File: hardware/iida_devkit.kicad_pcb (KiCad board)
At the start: 4 copper layers, 0 parts

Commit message: HW: Fix 3D models for components
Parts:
- added AE1: U.FL-R-SMT-1(10), Connector_Coaxial:U.FL_Hirose_U.FL-R-SMT-1_Vertical, F.Cu at (176.2, 138.7)
- added AE2: PCB antenna, PCB_antenna:800MHz_antenna, F.Cu at (163.4, 134.9)
- added C1: 4700 pF, Capacitor_SMD:C_0603_1608Metric_Pad1.08x0.95mm_HandSolder, F.Cu at (130.6, 115.9)
- added C10: 4.7 µF, Capacitor_SMD:C_0603_1608Metric_Pad1.08x0.95mm_HandSolder, F.Cu at (135.3, 61.2)
- added C11: 8 pF, Capacitor_SMD:C_0603_1608Metric_Pad1.08x0.95mm_HandSolder, F.Cu at (135.3, 63.7)
- added C12: 8 pF, Capacitor_SMD:C_0603_1608Metric_Pad1.08x0.95mm_HandSolder, F.Cu at (135.3, 66.2)
- added C13: 8 pF, Capacitor_SMD:C_0603_1608Metric_Pad1.08x0.95mm_HandSolder, F.Cu at (135.3, 68.8)
- added C14: 8 pF, Capacitor_SMD:C_0603_1608Metric_Pad1.08x0.95mm_HandSolder, F.Cu at (135.3, 71.3)
- added C15: 4.7 µF, Capacitor_SMD:C_0603_1608Metric_Pad1.08x0.95mm_HandSolder, F.Cu at (135.3, 73.8)
- added C16: 0.1 µF, Capacitor_SMD:C_0603_1608Metric_Pad1.08x0.95mm_HandSolder, F.Cu at (135.3, 76.3)
- added C17: 4.7 µF, Capacitor_SMD:C_0603_1608Metric_Pad1.08x0.95mm_HandSolder, F.Cu at (139.7, 61.2)
- added C18: 0.1 µF, Capacitor_SMD:C_0603_1608Metric_Pad1.08x0.95mm_HandSolder, F.Cu at (139.7, 63.7)
- added C19: 0.1 µF, Capacitor_SMD:C_0603_1608Metric_Pad1.08x0.95mm_HandSolder, F.Cu at (139.7, 66.2)
- added C2: 100 µF, Capacitor_SMD:CP_Elec_5x5.3, F.Cu at (139.5, 143.2)
- added C20: 4.7 µF, Capacitor_SMD:C_0603_1608Metric_Pad1.08x0.95mm_HandSolder, F.Cu at (139.7, 68.8)
- added C21: 0.1 µF, Capacitor_SMD:C_0603_1608Metric_Pad1.08x0.95mm_HandSolder, F.Cu at (139.7, 71.3)
- added C22: 0.1 µF, Capacitor_SMD:C_0603_1608Metric_Pad1.08x0.95mm_HandSolder, F.Cu at (139.7, 73.8)
- added C23: 0.1 µF, Capacitor_SMD:C_0603_1608Metric_Pad1.08x0.95mm_HandSolder, F.Cu at (139.7, 76.3)
- added C24: 0.1 µF, Capacitor_SMD:C_0603_1608Metric_Pad1.08x0.95mm_HandSolder, F.Cu at (181.7, 61.2)
- added C25: 68 pF, Capacitor_SMD:C_0603_1608Metric_Pad1.08x0.95mm_HandSolder, F.Cu at (181.7, 63.7)
- added C26: 15 pF, Capacitor_SMD:C_0603_1608Metric_Pad1.08x0.95mm_HandSolder, F.Cu at (181.7, 66.2)
- added C27: 0.1 µF, Capacitor_SMD:C_0603_1608Metric_Pad1.08x0.95mm_HandSolder, F.Cu at (181.7, 68.8)
- added C28: 0.01 µF, Capacitor_SMD:C_0603_1608Metric_Pad1.08x0.95mm_HandSolder, F.Cu at (181.7, 71.3)
- added C29: 0.1 µF, Capacitor_SMD:C_0603_1608Metric_Pad1.08x0.95mm_HandSolder, F.Cu at (181.7, 73.8)
- added C3: 0.1 µF, Capacitor_SMD:C_0603_1608Metric_Pad1.08x0.95mm_HandSolder, F.Cu at (130.6, 118.4)
- added C30: 0.1 µF, Capacitor_SMD:C_0603_1608Metric_Pad1.08x0.95mm_HandSolder, F.Cu at (186.1, 61.2)
- added C31: 10 µF, Capacitor_SMD:C_0603_1608Metric_Pad1.08x0.95mm_HandSolder, F.Cu at (186.1, 63.7)
- added C32: 0.1 µF, Capacitor_SMD:C_0603_1608Metric_Pad1.08x0.95mm_HandSolder, F.Cu at (186.1, 66.2)
- added C33: 33 pF, Capacitor_SMD:C_0603_1608Metric_Pad1.08x0.95mm_HandSolder, F.Cu at (183.2, 96.8)
- added C34: 33 pF, Capacitor_SMD:C_0603_1608Metric_Pad1.08x0.95mm_HandSolder, F.Cu at (183.2, 99.3)
- added C35: 33 pF, Capacitor_SMD:C_0603_1608Metric_Pad1.08x0.95mm_HandSolder, F.Cu at (183.2, 101.8)
- added C36: 33 pF, Capacitor_SMD:C_0603_1608Metric_Pad1.08x0.95mm_HandSolder, F.Cu at (183.2, 104.3)
- added C37: 0.1 µF, Capacitor_SMD:C_0603_1608Metric_Pad1.08x0.95mm_HandSolder, F.Cu at (183.2, 106.8)
- added C38: 33 pF, Capacitor_SMD:C_0603_1608Metric_Pad1.08x0.95mm_HandSolder, F.Cu at (181.2, 136.9)
- added C4: 0.1 µF, Capacitor_SMD:C_0603_1608Metric_Pad1.08x0.95mm_HandSolder, F.Cu at (130.6, 121.0)
- added C5: 0.1 µF, Capacitor_SMD:C_0603_1608Metric_Pad1.08x0.95mm_HandSolder, F.Cu at (130.6, 123.5)
- added C6: 4.7 µF, Capacitor_SMD:C_0603_1608Metric_Pad1.08x0.95mm_HandSolder, F.Cu at (130.6, 126.0)
- added C7: 4.7 µF, Capacitor_SMD:C_0603_1608Metric_Pad1.08x0.95mm_HandSolder, F.Cu at (130.6, 128.5)
- added C8: 4.7 µF, Capacitor_SMD:C_0603_1608Metric_Pad1.08x0.95mm_HandSolder, F.Cu at (134.9, 115.9)
- added C9: 4.7 µF, Capacitor_SMD:C_0603_1608Metric_Pad1.08x0.95mm_HandSolder, F.Cu at (134.9, 118.4)
- added D1: CDBA140LL-HF, Diode_SMD:D_SMA_Handsoldering, F.Cu at (123.4, 109.8)
- added D2: CDBA140LL-HF, Diode_SMD:D_SMA_Handsoldering, F.Cu at (123.4, 114.3)
- added D3: CDBA140LL-HF, Diode_SMD:D_SMA_Handsoldering, F.Cu at (123.4, 118.8)
- added D4: CDBA140LL-HF, Diode_SMD:D_SMA_Handsoldering, F.Cu at (123.4, 123.4)
- added D5: CDBA140LL-HF, Diode_SMD:D_SMA_Handsoldering, F.Cu at (123.4, 128.0)
- added F1: 3A, Fuse:Fuse_0805_2012Metric_Pad1.15x1.40mm_HandSolder, F.Cu at (120.7, 142.8)
- added F2: 3A, Fuse:Fuse_0805_2012Metric_Pad1.15x1.40mm_HandSolder, F.Cu at (120.7, 145.8)
- added FB1: 120 Ω @ 100 MHz, Resistor_SMD:R_0603_1608Metric_Pad0.98x0.95mm_HandSolder, F.Cu at (134.9, 121.0)
- added FB2: 120 Ω @ 100 MHz, Resistor_SMD:R_0603_1608Metric_Pad0.98x0.95mm_HandSolder, F.Cu at (144.0, 61.2)
- added FB3: 260 Ω @ 1 GHz, Resistor_SMD:R_0603_1608Metric_Pad0.98x0.95mm_HandSolder, F.Cu at (186.1, 68.8)
- added FID1: Fiducial, Fiducial:Fiducial_1mm_Mask2mm, F.Cu at (195.1, 97.3)
- added FID2: Fiducial, Fiducial:Fiducial_1mm_Mask2mm, F.Cu at (195.1, 100.9)
- added FID3: Fiducial, Fiducial:Fiducial_1mm_Mask2mm, F.Cu at (195.1, 104.4)
- added H1: MountingHole_Pad, MountingHole:MountingHole_2.2mm_M2_Pad_Via, F.Cu at (190.4, 98.5)
- added H2: MountingHole_Pad, MountingHole:MountingHole_2.2mm_M2_Pad_Via, F.Cu at (190.4, 104.5)
- added H3: MountingHole_Pad, MountingHole:MountingHole_2.2mm_M2_Pad_Via, F.Cu at (190.4, 110.4)
- added H4: MountingHole_Pad, MountingHole:MountingHole_2.2mm_M2_Pad_Via, F.Cu at (190.4, 116.4)
- added J1: B2B-PH-K-S, Connector_JST:JST_PH_B2B-PH-K_1x02_P2.00mm_Vertical, F.Cu at (147.0, 142.4)
- added J10: PRPC001DAAN-RC, Connector_PinHeader_2.54mm:PinHeader_1x02_P2.54mm_Vertical, F.Cu at (154.7, 91.3)
- added J11: PRPC006SAAN-RC, Connector_PinHeader_2.54mm:PinHeader_1x06_P2.54mm_Vertical, F.Cu at (157.5, 62.3)
- added J12: PRPC004SAAN-RC, Connector_PinHeader_2.54mm:PinHeader_1x04_P2.54mm_Vertical, F.Cu at (136.9, 94.8)
- added J13: PRPC001DAAN-RC, Connector_PinHeader_2.54mm:PinHeader_1x02_P2.54mm_Vertical, F.Cu at (194.9, 62.3)
- added J14: PRPC006SAAN-RC, Connector_PinHeader_2.54mm:PinHeader_1x06_P2.54mm_Vertical, F.Cu at (164.2, 97.9)
- added J15: G85D1160022HHR, G85D1160022HHR:AMPHENOL_G85D1160022HHR, F.Cu at (173.8, 104.2)
- added J2: USB4110-GF-A, Connector_USB:USB_C_Receptacle_GCT_USB4110, F.Cu at (142.3, 135.0)
- added J3: PRPC001DAAN-RC, Connector_PinHeader_2.54mm:PinHeader_1x02_P2.54mm_Vertical, F.Cu at (130.7, 109.8)
- added J4: PRPC001DAAN-RC, Connector_PinHeader_2.54mm:PinHeader_1x02_P2.54mm_Vertical, F.Cu at (135.4, 109.8)
- added J5: PRPC001DAAN-RC, Connector_PinHeader_2.54mm:PinHeader_1x02_P2.54mm_Vertical, F.Cu at (140.0, 109.8)
- added J6: PRPC001DAAN-RC, Connector_PinHeader_2.54mm:PinHeader_1x02_P2.54mm_Vertical, F.Cu at (144.7, 109.8)
- added J7: PRPC001DAAN-RC, Connector_PinHeader_2.54mm:PinHeader_1x02_P2.54mm_Vertical, F.Cu at (149.3, 109.8)
- added J8: SBH11-NBPC-D05-SM-BK, Connector_PinHeader_2.54mm:PinHeader_2x05_P2.54mm_Vertical_SMD, F.Cu at (134.8, 85.0)
- added J9: PRPC006SAAN-RC, Connector_PinHeader_2.54mm:PinHeader_1x06_P2.54mm_Vertical, F.Cu at (152.9, 62.3)
- added JP1: SolderJumper_3_Open, Jumper:SolderJumper-3_P2.0mm_Open_TrianglePad1.0x1.5mm, F.Cu at (170.1, 137.5)
- added L1: 2.7 µH, Inductor_SMD:L_Bourns-SRU8028_8.0x8.0mm, F.Cu at (147.1, 119.6)
- added L2: 39 nH, Inductor_SMD:L_0603_1608Metric_Pad1.05x0.95mm_HandSolder, F.Cu at (181.2, 139.4)
- added LED1: 150141YS73100, LED_SMD:LED_PLCC_2835_Handsoldering, F.Cu at (150.4, 126.7)
- added LED2: 150141YS73100, LED_SMD:LED_PLCC_2835_Handsoldering, F.Cu at (131.5, 94.6)
- added LED3: 150141YS73100, LED_SMD:LED_PLCC_2835_Handsoldering, F.Cu at (131.5, 99.0)
- added LED4: 150141YS73100, LED_SMD:LED_PLCC_2835_Handsoldering, F.Cu at (131.5, 103.3)
- added LED5: 150141YS73100, LED_SMD:LED_PLCC_2835_Handsoldering, F.Cu at (164.9, 89.7)
- added Q1: IRLML2246TRPBF, Package_TO_SOT_SMD:SC-59_Handsoldering, F.Cu at (131.7, 132.2)
- added Q2: DMN2046U-7, Package_TO_SOT_SMD:SC-59_Handsoldering, F.Cu at (131.7, 137.1)
- added Q3: DMN2046U-7, Package_TO_SOT_SMD:SC-59_Handsoldering, F.Cu at (131.7, 141.9)
- added Q4: IRLML2246TRPBF, Package_TO_SOT_SMD:SC-59_Handsoldering, F.Cu at (131.7, 146.7)
- added Q5: IRLML2246TRPBF, Package_TO_SOT_SMD:SC-59_Handsoldering, F.Cu at (190.0, 77.5)
- added Q6: MMBT3904, Package_TO_SOT_SMD:SC-59_Handsoldering, F.Cu at (190.0, 82.4)
- added R1: 1 MΩ, Resistor_SMD:R_1206_3216Metric_Pad1.30x1.75mm_HandSolder, F.Cu at (121.3, 136.4)
- added R10: 220 kΩ, Resistor_SMD:R_0603_1608Metric_Pad0.98x0.95mm_HandSolder, F.Cu at (139.3, 126.0)
- added R11: 20 Ω, Resistor_SMD:R_0603_1608Metric_Pad0.98x0.95mm_HandSolder, F.Cu at (144.0, 63.7)
- added R12: 20 Ω, Resistor_SMD:R_0603_1608Metric_Pad0.98x0.95mm_HandSolder, F.Cu at (144.0, 66.2)
- added R13: 0 Ω, Resistor_SMD:R_0805_2012Metric_Pad1.20x1.40mm_HandSolder, F.Cu at (130.8, 61.5)
- added R14: 0 Ω, Resistor_SMD:R_0805_2012Metric_Pad1.20x1.40mm_HandSolder, F.Cu at (130.8, 64.4)
- added R15: 2.2 kΩ, Resistor_SMD:R_0603_1608Metric_Pad0.98x0.95mm_HandSolder, F.Cu at (144.0, 68.8)
- added R16: 2.2 kΩ, Resistor_SMD:R_0603_1608Metric_Pad0.98x0.95mm_HandSolder, F.Cu at (144.0, 71.3)
- added R17: 20 Ω, Resistor_SMD:R_0603_1608Metric_Pad0.98x0.95mm_HandSolder, F.Cu at (144.0, 73.8)
- added R18: 20 Ω, Resistor_SMD:R_0603_1608Metric_Pad0.98x0.95mm_HandSolder, F.Cu at (144.0, 76.3)
- added R19: 10 kΩ, Resistor_SMD:R_0603_1608Metric_Pad0.98x0.95mm_HandSolder, F.Cu at (148.4, 61.2)
- added R2: 10 kΩ, Resistor_SMD:R_0603_1608Metric_Pad0.98x0.95mm_HandSolder, F.Cu at (134.9, 123.5)
- added R20: 0 Ω, Resistor_SMD:R_0805_2012Metric_Pad1.20x1.40mm_HandSolder, F.Cu at (130.8, 67.3)
- added R21: 0 Ω, Resistor_SMD:R_0805_2012Metric_Pad1.20x1.40mm_HandSolder, F.Cu at (130.8, 70.3)
- added R22: 0 Ω, Resistor_SMD:R_0805_2012Metric_Pad1.20x1.40mm_HandSolder, F.Cu at (130.8, 73.2)
- added R23: 0 Ω, Resistor_SMD:R_0805_2012Metric_Pad1.20x1.40mm_HandSolder, F.Cu at (130.8, 76.2)
- added R24: 2.2 kΩ, Resistor_SMD:R_0603_1608Metric_Pad0.98x0.95mm_HandSolder, F.Cu at (148.4, 63.7)
- added R25: 2.2 kΩ, Resistor_SMD:R_0603_1608Metric_Pad0.98x0.95mm_HandSolder, F.Cu at (148.4, 66.2)
- added R26: 2.2 kΩ, Resistor_SMD:R_0603_1608Metric_Pad0.98x0.95mm_HandSolder, F.Cu at (148.4, 68.8)
- added R27: 10 kΩ, Resistor_SMD:R_0603_1608Metric_Pad0.98x0.95mm_HandSolder, F.Cu at (186.1, 71.3)
- added R28: 2.2 kΩ, Resistor_SMD:R_0603_1608Metric_Pad0.98x0.95mm_HandSolder, F.Cu at (186.1, 73.8)
- added R29: 10 kΩ, Resistor_SMD:R_0603_1608Metric_Pad0.98x0.95mm_HandSolder, F.Cu at (190.4, 61.2)
- added R3: 5.1 kΩ, Resistor_SMD:R_0603_1608Metric_Pad0.98x0.95mm_HandSolder, F.Cu at (134.9, 126.0)
- added R30: 10 kΩ, Resistor_SMD:R_0603_1608Metric_Pad0.98x0.95mm_HandSolder, F.Cu at (190.4, 63.7)
- added R31: 2.2 kΩ, Resistor_SMD:R_0603_1608Metric_Pad0.98x0.95mm_HandSolder, F.Cu at (190.4, 66.2)
- added R32: 10 kΩ, Resistor_SMD:R_0603_1608Metric_Pad0.98x0.95mm_HandSolder, F.Cu at (190.4, 68.8)
- added R33: 10 kΩ, Resistor_SMD:R_0603_1608Metric_Pad0.98x0.95mm_HandSolder, F.Cu at (190.4, 71.3)
- added R34: 0 Ω, Resistor_SMD:R_0805_2012Metric_Pad1.20x1.40mm_HandSolder, F.Cu at (189.0, 86.2)
- added R35: 0 Ω, Resistor_SMD:R_0805_2012Metric_Pad1.20x1.40mm_HandSolder, F.Cu at (189.0, 89.1)
- added R36: 0 Ω, Resistor_SMD:R_0805_2012Metric_Pad1.20x1.40mm_HandSolder, F.Cu at (189.0, 92.1)
- added R37: 0 Ω, Resistor_SMD:R_0805_2012Metric_Pad1.20x1.40mm_HandSolder, F.Cu at (164.2, 137.1)
- added R38: 0 Ω, Resistor_SMD:R_0805_2012Metric_Pad1.20x1.40mm_HandSolder, F.Cu at (164.2, 140.1)
- added R39: 0 Ω, Resistor_SMD:R_0805_2012Metric_Pad1.20x1.40mm_HandSolder, F.Cu at (164.2, 143.0)
- added R4: 5.1 kΩ, Resistor_SMD:R_0603_1608Metric_Pad0.98x0.95mm_HandSolder, F.Cu at (134.9, 128.5)
- added R5: 330 Ω, Resistor_SMD:R_0603_1608Metric_Pad0.98x0.95mm_HandSolder, F.Cu at (139.3, 115.9)
- added R6: 2.2 kΩ, Resistor_SMD:R_0603_1608Metric_Pad0.98x0.95mm_HandSolder, F.Cu at (139.3, 118.4)
- added R7: 10 kΩ, Resistor_SMD:R_0603_1608Metric_Pad0.98x0.95mm_HandSolder, F.Cu at (139.3, 121.0)
- added R8: 2.2 kΩ, Resistor_SMD:R_0603_1608Metric_Pad0.98x0.95mm_HandSolder, F.Cu at (139.3, 123.5)
- added R9: 1 MΩ, Resistor_SMD:R_1206_3216Metric_Pad1.30x1.75mm_HandSolder, F.Cu at (121.3, 139.7)
- added SW_SPST1: PTS645SK50SMTR92 LFS, Button_Switch_SMD:SW_SPST_PTS645, F.Cu at (146.8, 93.0)
- added TP1: TestPoint, TestPoint:TestPoint_Pad_D1.5mm, F.Cu at (181.3, 76.8)
- added TP2: TestPoint, TestPoint:TestPoint_Pad_D1.5mm, F.Cu at (181.3, 80.4)
- added TP3: TestPoint, TestPoint:TestPoint_Pad_D1.5mm, F.Cu at (181.3, 83.9)
- added TP4: TestPoint, TestPoint:TestPoint_Pad_D1.5mm, F.Cu at (181.3, 87.5)
- added TP5: TestPoint, TestPoint:TestPoint_Pad_D1.5mm, F.Cu at (184.9, 76.8)
- added TP6: TestPoint, TestPoint:TestPoint_Pad_D1.5mm, F.Cu at (184.9, 80.4)
- added TP7: TestPoint, TestPoint:TestPoint_Pad_D1.5mm, F.Cu at (184.9, 83.9)
- added TVS1: SMAJ6.0CA-13-F, Diode_SMD:D_SMA_Handsoldering, F.Cu at (123.4, 132.5)
- added TVS10: SMAJ6.0CA-13-F, Diode_SMD:D_SMA_Handsoldering, F.Cu at (123.4, 98.7)
- added TVS11: SMAJ6.0CA-13-F, Diode_SMD:D_SMA_Handsoldering, F.Cu at (123.4, 103.2)
- added TVS12: CPDUC5V0USP-HF, Diode_SMD:D_0603_1608Metric_Pad1.05x0.95mm_HandSolder, F.Cu at (168.7, 113.3)
- added TVS13: CPDUC5V0USP-HF, Diode_SMD:D_0603_1608Metric_Pad1.05x0.95mm_HandSolder, F.Cu at (168.7, 115.9)
- added TVS14: CPDUC5V0USP-HF, Diode_SMD:D_0603_1608Metric_Pad1.05x0.95mm_HandSolder, F.Cu at (168.7, 118.5)
- added TVS15: CPDUC5V0USP-HF, Diode_SMD:D_0603_1608Metric_Pad1.05x0.95mm_HandSolder, F.Cu at (168.7, 121.1)
- added TVS2: SMAJ6.0CA-13-F, Diode_SMD:D_SMA_Handsoldering, F.Cu at (123.4, 62.2)
- added TVS3: SMAJ6.0CA-13-F, Diode_SMD:D_SMA_Handsoldering, F.Cu at (123.4, 66.8)
- added TVS4: SMAJ6.0CA-13-F, Diode_SMD:D_SMA_Handsoldering, F.Cu at (123.4, 71.3)
- added TVS5: SMAJ6.0CA-13-F, Diode_SMD:D_SMA_Handsoldering, F.Cu at (123.4, 75.9)
- added TVS6: SMAJ6.0CA-13-F, Diode_SMD:D_SMA_Handsoldering, F.Cu at (123.4, 80.5)
- added TVS7: SMAJ6.0CA-13-F, Diode_SMD:D_SMA_Handsoldering, F.Cu at (123.4, 85.0)
- added TVS8: SMAJ6.0CA-13-F, Diode_SMD:D_SMA_Handsoldering, F.Cu at (123.4, 89.5)
- added TVS9: SMAJ6.0CA-13-F, Diode_SMD:D_SMA_Handsoldering, F.Cu at (123.4, 94.1)
- added U1: USBLC6-2SC6, Package_TO_SOT_SMD:SOT-23-6_Handsoldering, F.Cu at (152.4, 132.2)
- added U10: SARA-R500S-61B, RF_GSM:ublox_SARA_LGA-96, F.Cu at (170.8, 73.8)
- added U2: S-8240ADQ-M6T1U, Package_TO_SOT_SMD:SOT-23-6_Handsoldering, F.Cu at (152.4, 137.0)
- added U3: MCP73811T-420I-OT, Package_TO_SOT_SMD:SOT-23-5_HandSoldering, F.Cu at (144.4, 127.0)
- added U4: TPS61023DRLR, Package_TO_SOT_SMD:SOT-563, F.Cu at (125.0, 143.1)
- added U5: AT25SF081B-SSHD-B, Package_SO:SOIC-8_3.9x4.9mm_P1.27mm, F.Cu at (145.5, 100.2)
- added U6: MCP9808, Package_SO:MSOP-8_3x3mm_P0.65mm, F.Cu at (153.4, 99.2)
- added U7: STM32L552CETx, Package_QFP:LQFP-48_7x7mm_P0.5mm, F.Cu at (146.9, 83.3)
- added U8: 74AVC1T45DW-7, Package_TO_SOT_SMD:SOT-363_SC-70-6_Handsoldering, F.Cu at (194.3, 86.7)
- added U9: 74AVC1T45DW-7, Package_TO_SOT_SMD:SOT-363_SC-70-6_Handsoldering, F.Cu at (194.3, 90.6)
- added Y1: ABS05-32.768KHZ-9-T, Crystal:Crystal_SMD_MicroCrystal_CM9V-T1A-2Pin_1.6x1.0mm_HandSoldering, F.Cu at (154.7, 84.8)
- added Y2: ECS-160-9-37-CKM-TR3, Crystal:Crystal_SMD_3225-4Pin_3.2x2.5mm_HandSoldering, F.Cu at (155.9, 80.5)

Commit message: HW: Layout power section
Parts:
- C9: value 4.7 µF -> 22 µF; footprint Capacitor_SMD:C_0603_1608Metric_Pad1.08x0.95mm_HandSolder -> Capacitor_SMD:C_0805_2012Metric_Pad1.18x1.45mm_HandSolder
- L1: value 2.7 µH -> 1 µH; footprint Inductor_SMD:L_Bourns-SRU8028_8.0x8.0mm -> Inductor_SMD:L_1008_2520Metric_Pad1.43x2.20mm_HandSolder
- R10: value 220 kΩ -> 100 kΩ
- R9: value 1 MΩ -> 453 kΩ; footprint Resistor_SMD:R_1206_3216Metric_Pad1.30x1.75mm_HandSolder -> Resistor_SMD:R_0603_1608Metric_Pad0.98x0.95mm_HandSolder
- U4: value TPS61023DRLR -> TPS62A01PDDCR; footprint Package_TO_SOT_SMD:SOT-563 -> Package_TO_SOT_SMD:SOT-23-6
- moved R4 172.3 mm to (277.7, 32.0), turned to 90 degrees
- moved R1 170.6 mm to (259.1, 35.8), turned to 180 degrees
- moved R3 169.6 mm to (276.1, 32.0), turned to 90 degrees
- moved J1 163.1 mm to (19.9, 40.1), turned to -90 degrees
- moved J2 161.0 mm to (268.5, 35.0)
- moved U1 156.2 mm to (268.5, 27.6), turned to 90 degrees
- moved C1 153.0 mm to (259.7, 33.8), turned to 180 degrees
- moved U2 151.7 mm to (39.2, 36.0), turned to 180 degrees
- moved F2 150.2 mm to (33.2, 23.8), turned to 90 degrees
- moved TVS1 149.4 mm to (22.8, 22.0)
- moved U3 147.7 mm to (31.9, 31.3), turned to 180 degrees
- moved Q4 147.7 mm to (39.8, 31.2), turned to -90 degrees
- moved C2 147.2 mm to (32.8, 41.8), turned to -90 degrees
- moved J3 143.7 mm to (20.0, 18.2), turned to 90 degrees
- moved FB1 143.2 mm to (29.8, 23.8), turned to -90 degrees
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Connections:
- L1 pad 1: Net-(D4-K) -> Net-(U4-SW)
- L1 pad 2: Net-(U4-SW) -> /Power/VOUT_{3V3}
- U4 pad 1: Net-(U4-FB) -> Net-(D4-K)
- U4 pad 2: Net-(D4-K) -> GND
- U4 pad 3: Net-(D4-K) -> Net-(U4-SW)
- U4 pad 4: GND -> Net-(D4-K)
- U4 pad 5: Net-(U4-SW) -> unconnected-(U4-PG-Pad5)
- U4 pad 6: /Power/VOUT_{3V3} -> Net-(U4-FB)
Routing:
- net Net-(J1-Pin_2): track 0.00 -> 30.3 mm
- net Net-(J2-CC1): track 0.00 -> 14.7 mm, vias 0 -> 2
- net GND: track 0.00 -> 10.7 mm, vias 0 -> 32
- net Net-(Q2-D): track 0.00 -> 10.5 mm
- net Net-(J2-CC2): track 0.00 -> 9.68 mm, vias 0 -> 2
- net Net-(Q3-G): track 0.00 -> 6.14 mm
- net Net-(D4-K): track 0.00 -> 5.58 mm
- net /Power/USB_DP_IN: track 0.00 -> 4.95 mm
- net +VBAT: track 0.00 -> 4.39 mm, vias 0 -> 3
- net /Power/USB_DN_IN: track 0.00 -> 4.27 mm
- net Net-(U1-VBUS): track 0.00 -> 3.93 mm, vias 0 -> 5
- net Net-(U2-VM): track 0.00 -> 2.03 mm
- net Net-(D4-A): track 0.00 -> 0.90 mm
- net Net-(D2-K): vias 0 -> 4
- added copper zone on F.Cu, net +VBAT
- added copper zone on F.Cu, net /Power/VOUT_{3V3}
- added copper zone on F.Cu, net GND
- added copper zone on F.Cu, net Net-(C2-Pad1)
- added copper zone on F.Cu, net Net-(C4-Pad1)
- added copper zone on F.Cu, net Net-(D1-A)
- added copper zone on F.Cu, net Net-(D1-K)
- added copper zone on F.Cu, net Net-(D2-A)
- added copper zone on B.Cu, net Net-(D2-K)
- added copper zone on F.Cu, net Net-(D2-K)
- added copper zone on F.Cu, net Net-(D3-A)
- added copper zone on F.Cu, net Net-(D4-A)
- added copper zone on F.Cu, net Net-(D4-K)
- added copper zone on F.Cu, net Net-(J1-Pin_1)
- added copper zone on F.Cu, net Net-(J1-Pin_2)
- added copper zone on F.Cu, net Net-(J2-SHIELD)
- added copper zone on F.Cu, net Net-(Q2-G)
- added copper zone on F.Cu, net Net-(U1-VBUS)
- added copper zone on F.Cu, net Net-(U4-FB)
- added copper zone on F.Cu, net Net-(U4-SW)

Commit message: HW: Layout SIM section
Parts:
- moved J15 112.0 mm to (274.6, 153.0), turned to 90 degrees
- moved J14 104.4 mm to (256.2, 147.1)
- moved TVS12 103.3 mm to (265.8, 148.8), turned to 90 degrees
- moved TVS15 103.2 mm to (265.4, 157.2), turned to -90 degrees
- moved TVS13 99.9 mm to (262.6, 150.1), turned to 90 degrees
- moved TVS14 99.1 mm to (260.6, 155.6), turned to -90 degrees
- moved C36 96.4 mm to (263.8, 157.2), turned to -90 degrees
- moved C33 96.2 mm to (264.2, 148.8), turned to 90 degrees
- moved C37 93.7 mm to (262.2, 157.2), turned to -90 degrees
- moved C35 92.9 mm to (259.0, 155.6), turned to -90 degrees
- moved C34 92.9 mm to (261.0, 150.1), turned to 90 degrees
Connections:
- J15 pad C1: (no net) -> /Modem/VSIM
- J15 pad C2: (no net) -> /Modem/SIM_RST
- J15 pad C3: (no net) -> /Modem/SIM_CLK
- J15 pad C5: (no net) -> GND
- J15 pad C6: (no net) -> unconnected-(J15-VPP-PadC6)
- J15 pad C7: (no net) -> /Modem/SIM_IO
- J15 pad S1: (no net) -> GND
- J15 pad S2: (no net) -> GND
- J15 pad S3: (no net) -> GND
- J15 pad SW: (no net) -> unconnected-(J15-PadSW)
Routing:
- net GND: vias 32 -> 38

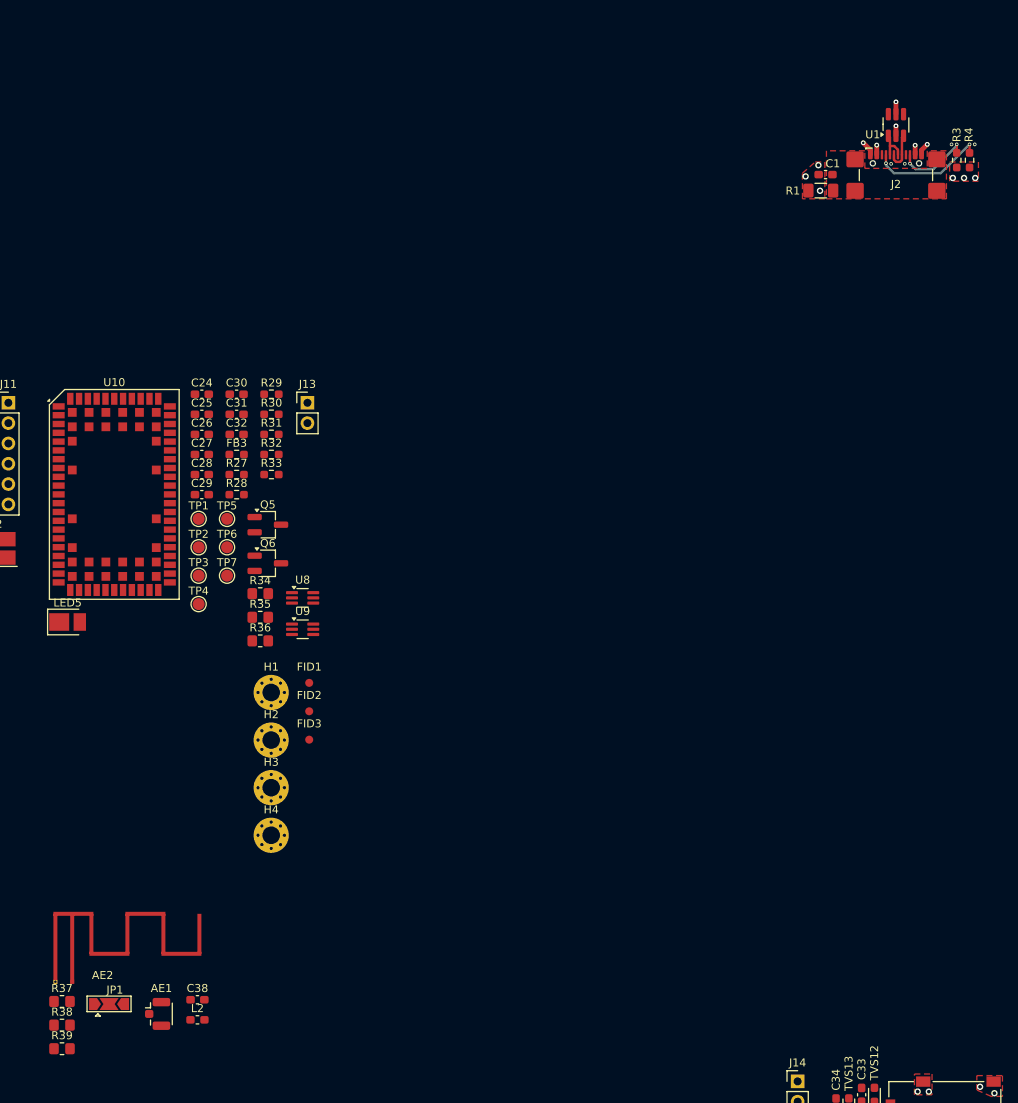
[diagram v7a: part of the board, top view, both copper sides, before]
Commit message: HW: Layout antenna section
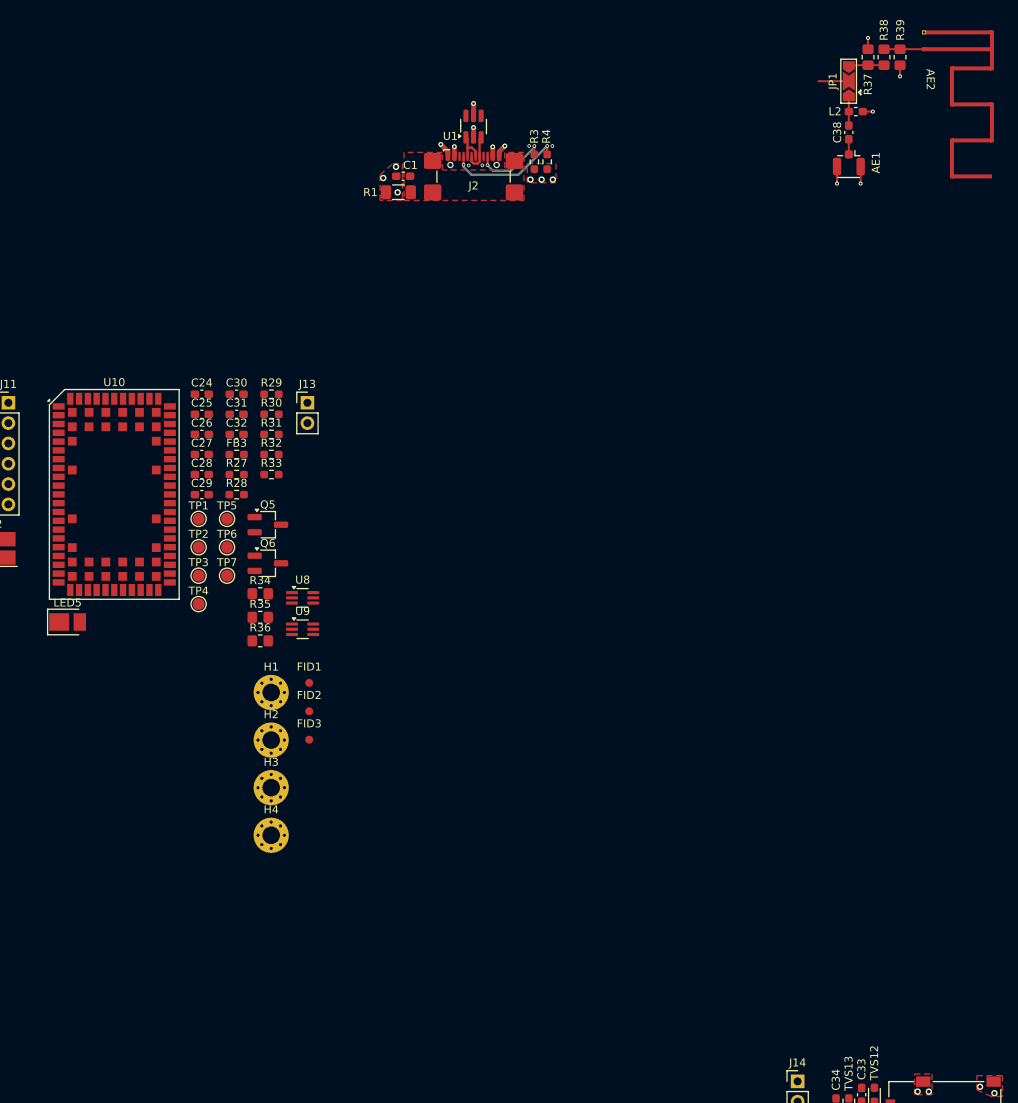
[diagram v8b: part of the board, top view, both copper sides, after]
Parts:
- moved R39 162.3 mm to (269.0, 19.1), turned to 90 degrees
- moved AE2 160.9 mm to (271.8, 16.0), turned to -90 degrees
- moved R38 158.7 mm to (267.0, 19.1), turned to -90 degrees
- moved R37 155.2 mm to (265.0, 19.1), turned to -90 degrees
- moved JP1 147.8 mm to (262.6, 22.1), turned to 90 degrees
- moved L2 140.2 mm to (263.5, 25.9)
- moved AE1 137.1 mm to (262.6, 32.3), turned to -90 degrees
- moved C38 135.6 mm to (262.6, 28.5), turned to 90 degrees
- moved C1 52.8 mm to (206.9, 34.0)
- moved J2 52.8 mm to (215.7, 35.2)
- moved R4 52.8 mm to (224.9, 32.2)
- moved U1 52.8 mm to (215.7, 27.8)
- moved R1 52.8 mm to (206.3, 36.0)
- moved R3 52.8 mm to (223.3, 32.2)
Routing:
- net GND: track 10.7 -> 19.0 mm, vias 38 -> 43
- net /Antenna/ANT_PCB: track 0.00 -> 5.00 mm
- net /Antenna/ANT_PCB_SEL: track 0.00 -> 4.40 mm
- net /Antenna/ANT: track 0.00 -> 3.80 mm
- net /Antenna/ANT_EXT_SEL: track 0.00 -> 3.54 mm
- net /Antenna/ANT_EXT: track 0.00 -> 1.89 mm
